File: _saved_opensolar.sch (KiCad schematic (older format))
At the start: 150 parts, among them P1 USB_OTG, P2 microSD, P3 Panel+, P4 Panel-, P5 Batt-, P6 Batt+, Q1 IPP076N12N3, Q2 IPP076N12N3, Q3 IPP076N12N3, Q4 IPP076N12N3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

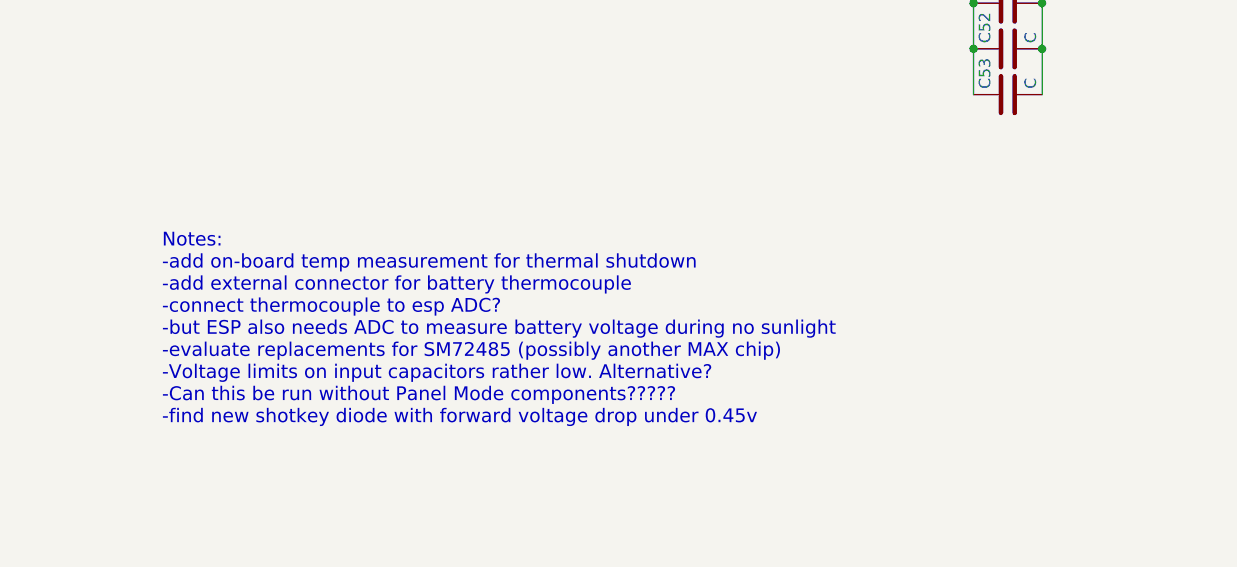
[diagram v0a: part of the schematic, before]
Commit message: esp adc Vout
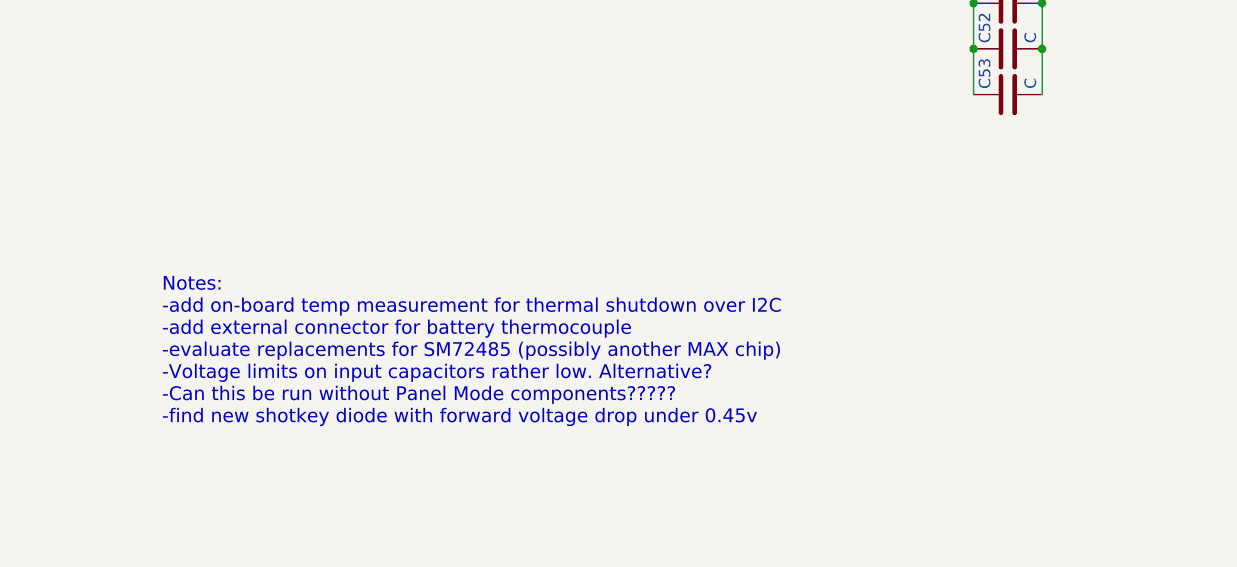
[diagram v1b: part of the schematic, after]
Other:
- note added: "Notes:\n-add on-board temp measurement for thermal shutdown over I2C\n-add external connector for battery thermocouple\n-evaluate replacements for SM72485 (possibly another MAX chip)\n-Voltage limits on input capacitors rather low. Alternative?\n-Can this be run without Panel Mode components?????\n-find new shotkey diode with forward voltage drop under 0.45v\n"
- note removed: "Notes:\n-add on-board temp measurement for thermal shutdown\n-add external connector for battery thermocouple\n-connect thermocouple to esp ADC?\n-but ESP also needs ADC to measure battery voltage during no sunlight\n-evaluate replacements for SM72485 (possibly another MAX chip)\n-Voltage limits on input capacitors rather low. Alternative?\n-Can this be run without Panel Mode components?????\n-fi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"
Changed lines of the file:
@@
 3v3 @ 500mA\nAlways on\nPowered off batteries\nMax 76 volts input\nMin 7.5 volts input
 Text Notes 6500 5550 0    60   ~ 0
-Notes:\n-add on-board temp measurement for thermal shutdown\n-add external connector for battery thermocouple\n-connect thermocouple to esp ADC?\n-but ESP also needs ADC to measure battery voltage during no sunlight\n-evaluate replacements for SM72485 (possibly another MAX chip)\n-Voltage limits on input capacitors rather low. Alternative?\n-Can this be run without Panel Mode components?????\n-find new shotkey diode with forward voltage drop under 0.45v\n
+Notes:\n-add on-board temp measurement for thermal shutdown over I2C\n-add external connector for battery thermocouple\n-evaluate replacements for SM72485 (possibly another MAX chip)\n-Voltage limits on input capacitors rather low. Alternative?\n-Can this be run without Panel Mode components?????\n-find new shotkey diode with forward voltage drop under 0.45v\n
 $Comp
 L C C59
